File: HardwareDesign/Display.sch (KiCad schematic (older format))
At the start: 31 parts, among them J601 Conn_01x12, U601 Upduino_3.0, U602 IDT7201, U603 74LVC245, U604 74LVC245

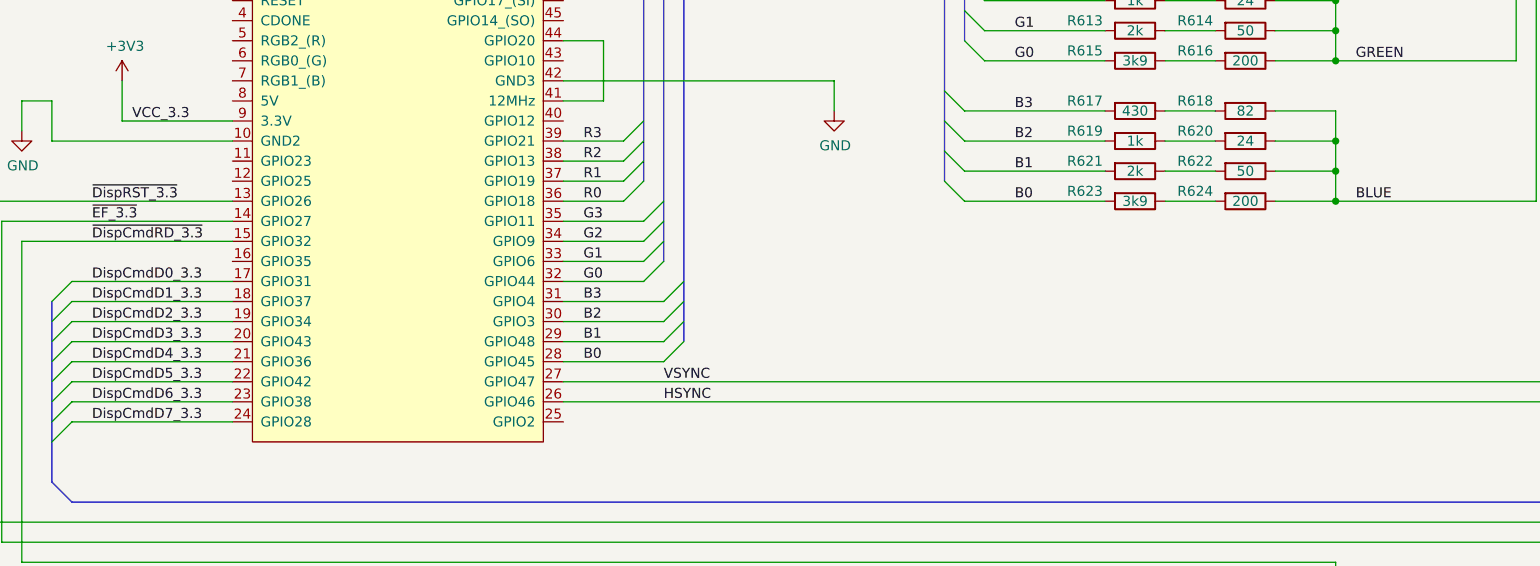
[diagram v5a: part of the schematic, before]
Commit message: add debug LEDs
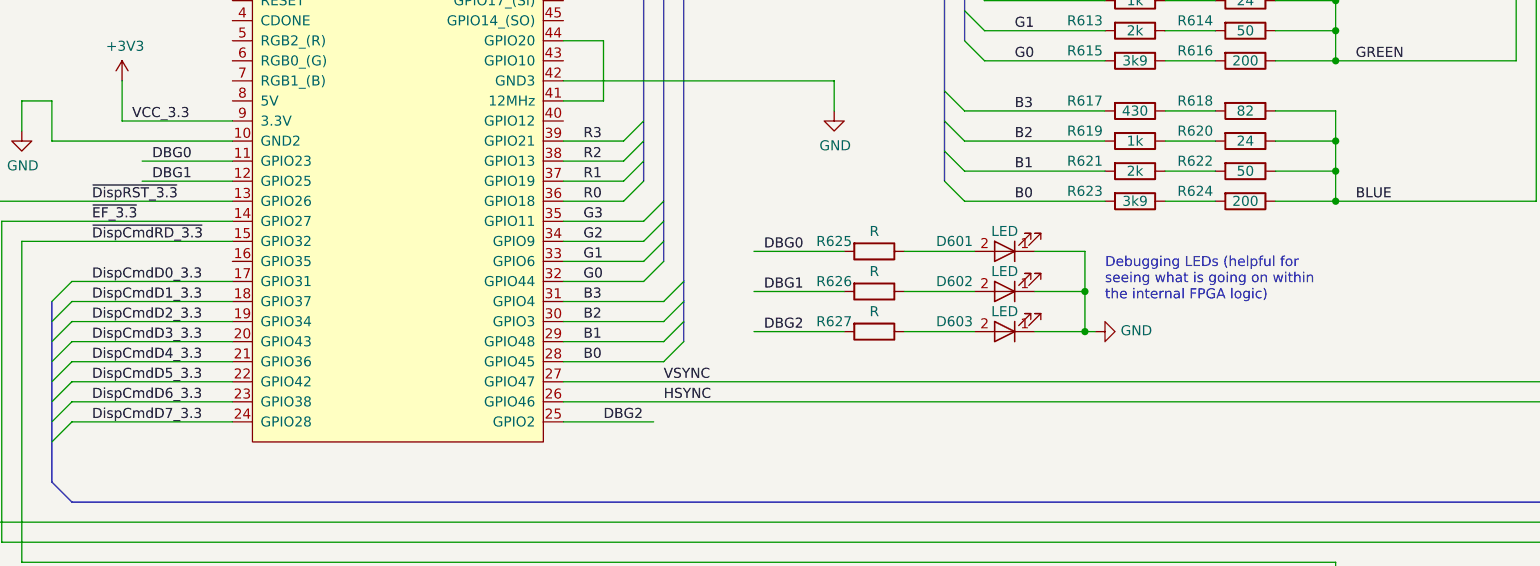
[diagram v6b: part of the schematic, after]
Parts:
- added D601, D602, D603: LED, symbol device:LED
- added R625, R626, R627: R, symbol device:R
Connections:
- net labels added: DBG0, DBG1, DBG2
- wire segments 224 -> 239
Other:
- note added: "Debugging LEDs (helpful for\nseeing what is going on within\nthe internal FPGA logic)"
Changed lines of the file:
@@
 Wire Wire Line
 	6250 7850 6250 7700
+$Comp
+L power:VCC #PWR?
+U 1 1 61D694BA
+P 6250 7700
+F 0 "#PWR?" H 6250 7550 50  0001 C CNN
+F 1 "VCC" H 6267 7873 50  0000 C CNN
+F 2 "" H 6250 7700 50  0001 C CNN
+F 3 "" H 6250 7700 50  0001 C CNN
+	1    6250 7700
+	1    0    0    -1
+$EndComp
+$Comp
+L device:LED D601
+U 1 1 62C6CE09
+P 5650 2950
+F 0 "D601" H 5900 2900 50  0000 C CNN
+F 1 "LED" H 5650 2850 50  0000 C CNN
+F 2 "" H 5650 2950 50  0001 C CNN
+F 3 "" H 5650 2950 50  0001 C CNN
+	1    5650 2950
+	-1   0    0    1
+$EndComp
+$Comp
+L device:LED D602
+U 1 1 62C6DBC0
+P 5650 3150
+F 0 "D602" H 5900 3100 50  0000 C CNN
+F 1 "LED" H 5650 3050 50  0000 C CNN
+F 2 "" H 5650 3150 50  0001 C CNN
+F 3 "" H 5650 3150 50  0001 C CNN
+	1    5650 3150
+	-1   0    0    1
+$EndComp
+$Comp
+L device:LED D603
+U 1 1 62C90E00
+P 5650 3350
+F 0 "D603" H 5900 3300 50  0000 C CNN
+F 1 "LED" H 5650 3250 50  0000 C CNN
+F 2 "" H 5650 3350 50  0001 C CNN
+F 3 "" H 5650 3350 50  0001 C CNN
+	1    5650 3350
+	-1   0    0    1
+$EndComp
+$Comp
+L device:R R625
+U 1 1 62CA2E1D
+P 5000 2950
+F 0 "R625" V 4950 2750 50  0000 C CNN
+F 1 "R" V 4900 2950 50  0000 C CNN
+F 2 "" V 4930 2950 50  0001 C CNN
+F 3 "" H 5000 2950 50  0001 C CNN
+	1    5000 2950
+	0    1    1    0
+$EndComp
+$Comp
+L device:R R626
+U 1 1 62CE9D70
+P 5000 3150
+F 0 "R626" V 4950 2950 50  0000 C CNN
+F 1 "R" V 4900 3150 50  0000 C CNN
+F 2 "" V 4930 3150 50  0001 C CNN
+F 3 "" H 5000 3150 50  0001 C CNN
+	1    5000 3150
+	0    1    1    0
+$EndComp
+$Comp
+L device:R R627
+U 1 1 62CFB62E
+P 5000 3350
+F 0 "R627" V 4950 3150 50  0000 C CNN
+F 1 "R" V 4900 3350 50  0000 C CNN
+F 2 "" V 4930 3350 50  0001 C CNN
+F 3 "" H 5000 3350 50  0001 C CNN
+	1    5000 3350
+	0    1    1    0
+$EndComp
+Wire Wire Line
+	4400 2950 4850 2950
+Wire Wire Line
+	4400 3150 4850 3150
+Wire Wire Line
+	4400 3350 4850 3350
+$Comp
+L power:GND #PWR?
+U 1 1 62D67C00
+P 6100 3350
+F 0 "#PWR?" H 6100 3100 50  0001 C CNN
+F 1 "GND" V 6105 3222 50  0000 R CNN
+F 2 "" H 6100 3350 50  0001 C CNN
+F 3 "" H 6100 3350 50  0001 C CNN
+	1    6100 3350
+	0    -1   -1   0
+$EndComp
+Wire Wire Line
+	5800 3350 6050 3350
+Wire Wire Line
+	5800 2950 6050 2950
+Wire Wire Line
+	6050 2950 6050 3150
+Connection ~ 6050 3350
+Wire Wire Line
+	6050 3350 6100 3350
+Wire Wire Line
+	5800 3150 6050 3150
+Connection ~ 6050 3150
+Wire Wire Line
+	6050 3150 6050 3350
+Wire Wire Line
+	5150 2950 5500 2950
+Wire Wire Line
+	5150 3150 5500 3150
+Wire Wire Line
+	5150 3350 5500 3350
+Text Label 4450 2950 0    50   ~ 0
+DBG0
+Text Label 4450 3150 0    50   ~ 0
+DBG1
+Text Label 4450 3350 0    50   ~ 0
+DBG2
+Wire Wire Line
+	1800 2500 1350 2500
+Wire Wire Line
+	1800 2600 1350 2600
+Text Label 1400 2500 0    50   ~ 0
+DBG0
+Text Label 1400 2600 0    50   ~ 0
+DBG1
+Wire Wire Line
+	3450 3800 3900 3800
+Text Label 3650 3800 0    50   ~ 0
+DBG2
+Text Notes 6150 3200 0    50   ~ 0
+Debugging LEDs (helpful for\nseeing what is going on within\nthe internal FPGA logic)
 Wire Bus Line
 	3400 6050 3400 8400
@@
 	750  6750 750  8400
 Wire Bus Line
+	900  3200 900  4100
+Wire Bus Line
 	10000 4300 10000 7100
 Wire Bus Line
 	3750 6050 3750 7000
-Wire Bus Line
-	900  3200 900  4100
-$Comp
-L power:VCC #PWR?
-U 1 1 61D694BA
-P 6250 7700
-F 0 "#PWR?" H 6250 7550 50  0001 C CNN
-F 1 "VCC" H 6267 7873 50  0000 C CNN
-F 2 "" H 6250 7700 50  0001 C CNN
-F 3 "" H 6250 7700 50  0001 C CNN
-	1    6250 7700
-	1    0    0    -1
-$EndComp
 $EndSCHEMATC
